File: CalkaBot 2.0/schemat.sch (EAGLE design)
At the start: 41 parts, among them IC1 TB6612FNG, IC2 LM339D, Q1 16MHz, X1 MINI-USB-32005-301

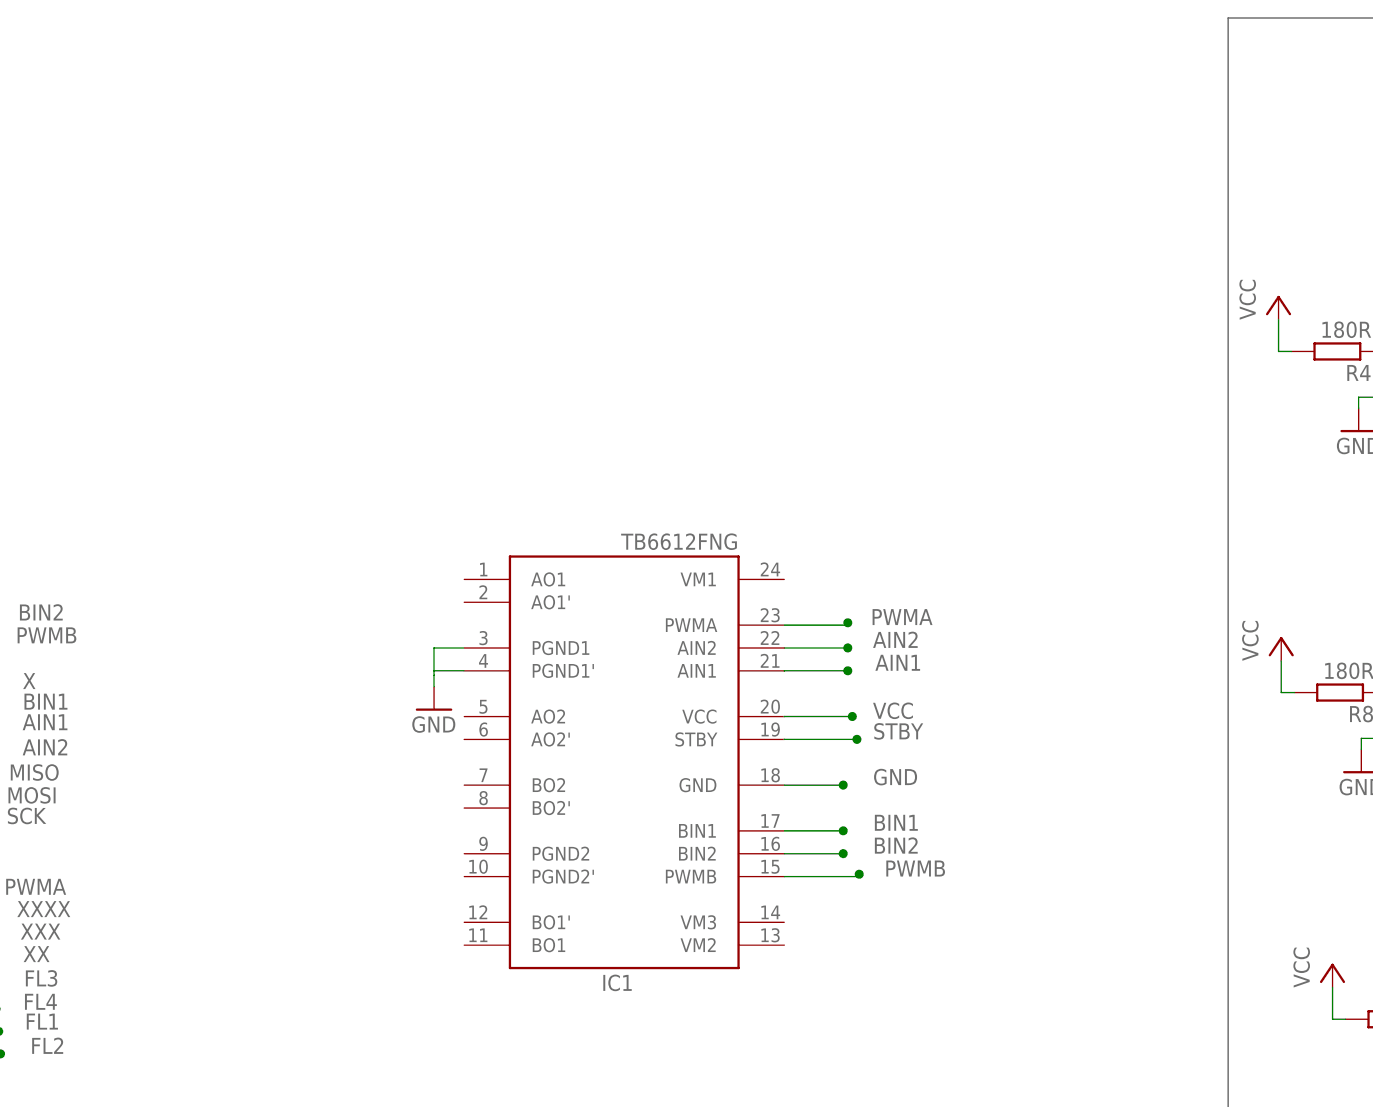
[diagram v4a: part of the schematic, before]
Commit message: Dodałem filtr do zasialania silników i do sterownika
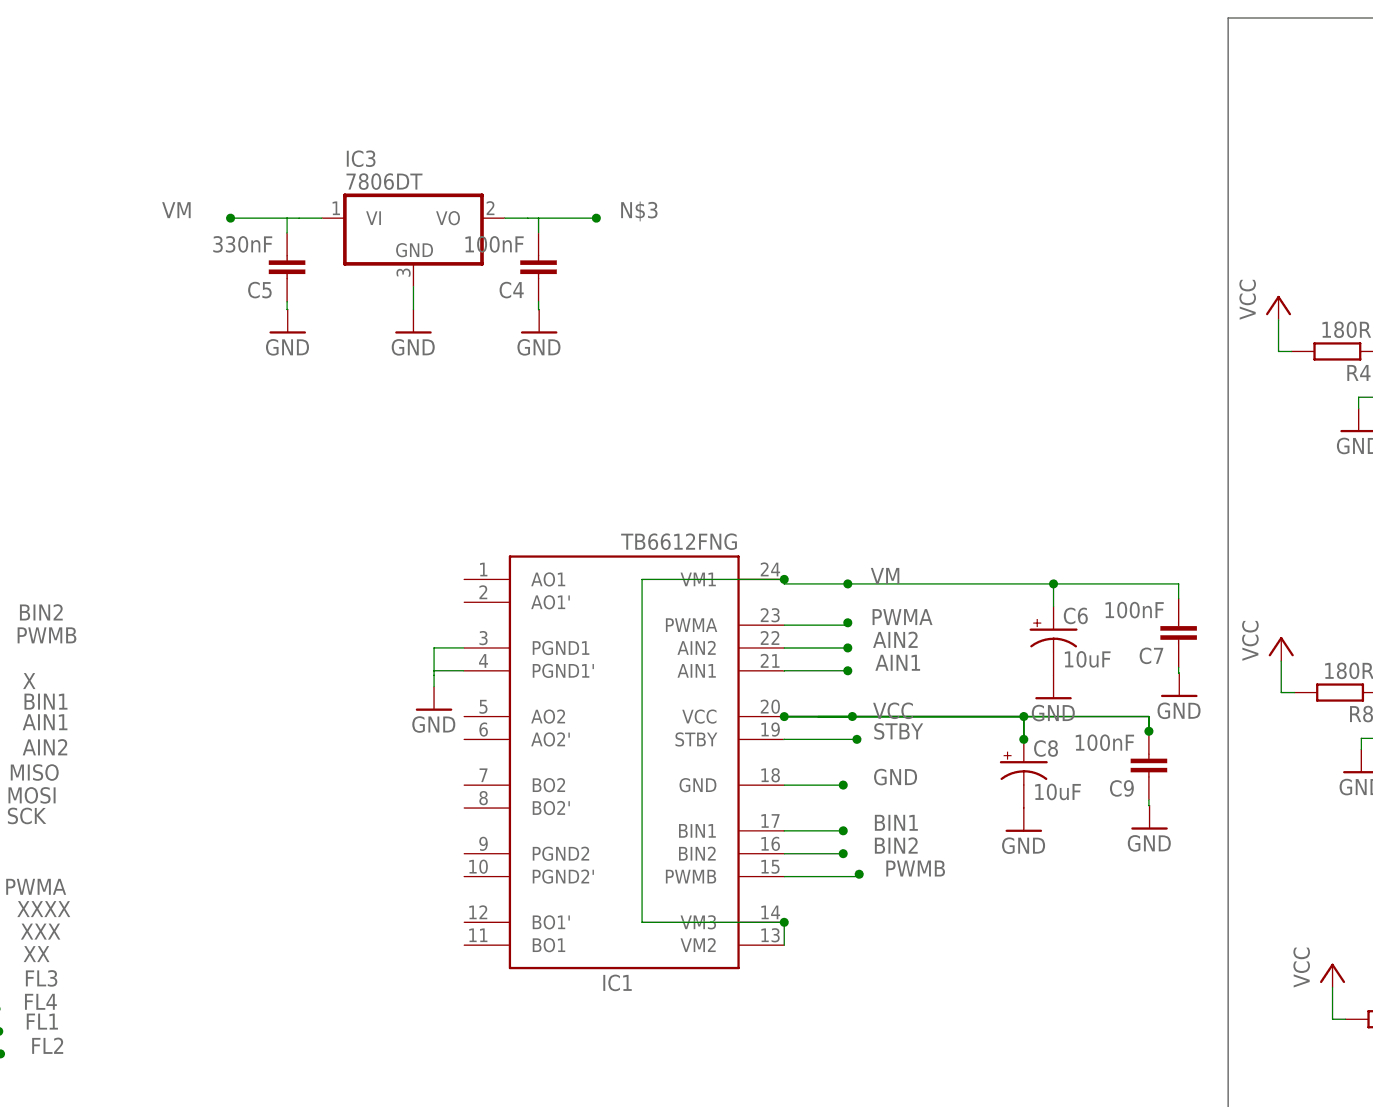
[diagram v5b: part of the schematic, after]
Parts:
- added C4, C7, C9: 100nF, rcl:C-EUC0805
- added C5: 330nF, rcl:C-EUC0805
- added C6, C8: 10uF, rcl:CPOL-USUD-4X5,8
- added IC3: 7806DT, linear3:7806DT
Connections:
- new net N$3: C4.2, IC3.VO
- new net VM: C5.2, C6.+, C7.2, IC1.VM1, IC1.VM2, IC1.VM3, IC3.VI
- net GND: now also C4.1, C5.1, C6.-, C7.1, C8.-, C9.1, IC3.GND
- net VCC: now also C8.+, C9.2
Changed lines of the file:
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@@
 <part name="R9" library="rcl" library_urn="urn:adsk.eagle:library:334" deviceset="R-EU_" device="R0805" package3d_urn="urn:adsk.eagle:package:23553/2" value="10k"/>
 <part name="RESETBUTTON3" library="switch-omron" library_urn="urn:adsk.eagle:library:377" deviceset="10-XX" device="" package3d_urn="urn:adsk.eagle:package:27496/1"/>
+<part name="IC3" library="linear3" deviceset="78*" device="DT" technology="06"/>
+<part name="GND7" library="supply1" library_urn="urn:adsk.eagle:library:371" deviceset="GND" device=""/>
+<part name="C4" library="rcl" library_urn="urn:adsk.eagle:library:334" deviceset="C-EU" device="C0805" package3d_urn="urn:adsk.eagle:package:23617/2" value="100nF"/>
+<part name="C5" library="rcl" library_urn="urn:adsk.eagle:library:334" deviceset="C-EU" device="C0805" package3d_urn="urn:adsk.eagle:package:23617/2" value="330nF"/>
+<part name="GND10" library="supply1" library_urn="urn:adsk.eagle:library:371" deviceset="GND" device=""/>
+<part name="GND13" library="supply1" library_urn="urn:adsk.eagle:library:371" deviceset="GND" device=""/>
+<part name="C6" library="rcl" library_urn="urn:adsk.eagle:library:334" deviceset="CPOL-US" device="UD-4X5,8" package3d_urn="urn:adsk.eagle:package:23474/1" value="10uF"/>
+<part name="C7" library="rcl" library_urn="urn:adsk.eagle:library:334" deviceset="C-EU" device="C0805" package3d_urn="urn:adsk.eagle:package:23617/2" value="100nF"/>
+<part name="GND14" library="supply1" library_urn="urn:adsk.eagle:library:371" deviceset="GND" device=""/>
+<part name="GND15" library="supply1" library_urn="urn:adsk.eagle:library:371" deviceset="GND" device=""/>
+<part name="C8" library="rcl" library_urn="urn:adsk.eagle:library:334" deviceset="CPOL-US" device="UD-4X5,8" package3d_urn="urn:adsk.eagle:package:23474/1" value="10uF"/>
+<part name="C9" library="rcl" library_urn="urn:adsk.eagle:library:334" deviceset="C-EU" device="C0805" package3d_urn="urn:adsk.eagle:package:23617/2" value="100nF"/>
+<part name="GND16" library="supply1" library_urn="urn:adsk.eagle:library:371" deviceset="GND" device=""/>
+<part name="GND17" library="supply1" library_urn="urn:adsk.eagle:library:371" deviceset="GND" device=""/>
 </parts>
 <sheets>
@@
 <instance part="R9" gate="G$1" x="21.082" y="-0.508"/>
 <instance part="RESETBUTTON3" gate="1" x="21.22" y="-10.26" rot="R90"/>
+<instance part="IC3" gate="A1" x="68.58" y="124.46"/>
+<instance part="GND7" gate="1" x="68.58" y="111.76"/>
+<instance part="C4" gate="G$1" x="82.48" y="117.74" rot="R180"/>
+<instance part="C5" gate="G$1" x="54.54" y="117.74" rot="R180"/>
+<instance part="GND10" gate="1" x="82.55" y="111.76"/>
+<instance part="GND13" gate="1" x="54.61" y="111.76"/>
+<instance part="C6" gate="G$1" x="139.7" y="78.74"/>
+<instance part="C7" gate="G$1" x="153.6" y="77.1" rot="R180"/>
+<instance part="GND14" gate="1" x="139.7" y="71.12"/>
+<instance part="GND15" gate="1" x="153.67" y="71.374"/>
+<instance part="C8" gate="G$1" x="136.398" y="64.008"/>
+<instance part="C9" gate="G$1" x="150.298" y="62.368" rot="R180"/>
+<instance part="GND16" gate="1" x="136.398" y="56.388"/>
+<instance part="GND17" gate="1" x="150.368" y="56.642"/>
 </instances>
 <busses>
@@
 <junction x="-93.08" y="-7.72"/>
 </segment>
+<segment>
+<pinref part="IC3" gate="A1" pin="GND"/>
+<wire x1="68.58" y1="116.84" x2="68.58" y2="114.3" width="0.1524" layer="91"/>
+<pinref part="GND7" gate="1" pin="GND"/>
+</segment>
+<segment>
+<pinref part="GND13" gate="1" pin="GND"/>
+<pinref part="C5" gate="G$1" pin="1"/>
+<wire x1="54.61" y1="114.3" x2="54.54" y2="114.3" width="0.1524" layer="91"/>
+<wire x1="54.54" y1="114.3" x2="54.54" y2="115.2" width="0.1524" layer="91"/>
+</segment>
+<segment>
+<pinref part="GND10" gate="1" pin="GND"/>
+<pinref part="C4" gate="G$1" pin="1"/>
+<wire x1="82.55" y1="114.3" x2="82.48" y2="114.3" width="0.1524" layer="91"/>
+<wire x1="82.48" y1="114.3" x2="82.48" y2="115.2" width="0.1524" layer="91"/>
+</segment>
+<segment>
+<pinref part="C6" gate="G$1" pin="-"/>
+<pinref part="GND14" gate="1" pin="GND"/>
+</segment>
+<segment>
+<pinref part="C7" gate="G$1" pin="1"/>
+<pinref part="GND15" gate="1" pin="GND"/>
+<wire x1="153.6" y1="74.56" x2="153.6" y2="73.914" width="0.1524" layer="91"/>
+<wire x1="153.6" y1="73.914" x2="153.67" y2="73.914" width="0.1524" layer="91"/>
+</segment>
+<segment>
+<pinref part="C8" gate="G$1" pin="-"/>
+<pinref part="GND16" gate="1" pin="GND"/>
+</segment>
+<segment>
+<pinref part="C9" gate="G$1" pin="1"/>
+<pinref part="GND17" gate="1" pin="GND"/>
+<wire x1="150.298" y1="59.828" x2="150.298" y2="59.182" width="0.1524" layer="91"/>
+<wire x1="150.298" y1="59.182" x2="150.368" y2="59.182" width="0.1524" layer="91"/>
+</segment>
 </net>
 <net name="D-" class="0">
@@
 <junction x="117.348" y="69.088"/>
 <label x="119.634" y="68.834" size="1.778" layer="95"/>
+<wire x1="109.78" y1="69.08" x2="139.7" y2="69.08" width="0.1524" layer="91"/>
+<wire x1="113.538" y1="69.088" x2="136.398" y2="69.088" width="0.1524" layer="91"/>
+<wire x1="136.398" y1="69.088" x2="150.298" y2="69.088" width="0.1524" layer="91"/>
+<wire x1="136.398" y1="69.088" x2="136.398" y2="66.548" width="0.1524" layer="91"/>
+<junction x="136.398" y="69.088"/>
+<pinref part="C8" gate="G$1" pin="+"/>
+<pinref part="C9" gate="G$1" pin="2"/>
+<wire x1="150.298" y1="67.448" x2="150.298" y2="69.088" width="0.1524" layer="91"/>
+<wire x1="109.78" y1="69.08" x2="136.398" y2="69.08" width="0.1524" layer="91"/>
+<wire x1="136.398" y1="69.08" x2="136.398" y2="66.548" width="0.1524" layer="91"/>
+<junction x="109.78" y="69.08"/>
+<junction x="136.398" y="66.548"/>
+<wire x1="109.78" y1="69.08" x2="150.298" y2="69.08" width="0.1524" layer="91"/>
+<wire x1="150.298" y1="69.08" x2="150.298" y2="67.448" width="0.1524" layer="91"/>
+<junction x="150.298" y="67.448"/>
 </segment>
 <segment>
@@
 </segment>
 </net>
+<net name="N$3" class="0">
+<segment>
+<pinref part="IC3" gate="A1" pin="VO"/>
+<pinref part="C4" gate="G$1" pin="2"/>
+<wire x1="78.74" y1="124.46" x2="81.28" y2="124.46" width="0.1524" layer="91"/>
+<wire x1="81.28" y1="124.46" x2="82.48" y2="124.46" width="0.1524" layer="91"/>
+<wire x1="82.48" y1="124.46" x2="82.48" y2="122.82" width="0.1524" layer="91"/>
+<wire x1="82.48" y1="124.46" x2="88.9" y2="124.46" width="0.1524" layer="91"/>
+<junction x="88.9" y="124.46"/>
+<label x="91.44" y="124.46" size="1.778" layer="95"/>
+</segment>
+</net>
+<net name="VM" class="0">
+<segment>
+<pinref part="C5" gate="G$1" pin="2"/>
+<pinref part="IC3" gate="A1" pin="VI"/>
+<wire x1="54.54" y1="122.82" x2="54.54" y2="124.46" width="0.1524" layer="91"/>
+<wire x1="54.54" y1="124.46" x2="55.88" y2="124.46" width="0.1524" layer="91"/>
+<wire x1="55.88" y1="124.46" x2="58.42" y2="124.46" width="0.1524" layer="91"/>
+<wire x1="54.54" y1="124.46" x2="48.26" y2="124.46" width="0.1524" layer="91"/>
+<junction x="48.26" y="124.46"/>
+<label x="40.64" y="124.46" size="1.778" layer="95"/>
+</segment>
+<segment>
+<pinref part="IC1" gate="G$1" pin="VM1"/>
+<wire x1="109.78" y1="84.32" x2="109.78" y2="83.82" width="0.1524" layer="91"/>
+<wire x1="109.78" y1="83.82" x2="116.84" y2="83.82" width="0.1524" layer="91"/>
+<junction x="116.84" y="83.82"/>
+<label x="119.38" y="83.82" size="1.778" layer="95"/>
+<wire x1="116.84" y1="83.82" x2="139.7" y2="83.82" width="0.1524" layer="91"/>
+<wire x1="139.7" y1="83.82" x2="153.6" y2="83.82" width="0.1524" layer="91"/>
+<wire x1="139.7" y1="83.82" x2="139.7" y2="81.28" width="0.1524" layer="91"/>
+<junction x="139.7" y="83.82"/>
+<pinref part="C6" gate="G$1" pin="+"/>
+<pinref part="C7" gate="G$1" pin="2"/>
+<wire x1="153.6" y1="82.18" x2="153.6" y2="83.82" width="0.1524" layer="91"/>
+<wire x1="109.78" y1="84.32" x2="93.98" y2="84.32" width="0.1524" layer="91"/>
+<junction x="109.78" y="84.32"/>
+<pinref part="IC1" gate="G$1" pin="VM2"/>
+<pinref part="IC1" gate="G$1" pin="VM3"/>
+<wire x1="109.78" y1="46.22" x2="109.78" y2="43.68" width="0.1524" layer="91"/>
+<wire x1="93.98" y1="84.32" x2="93.98" y2="46.22" width="0.1524" layer="91"/>
+<wire x1="93.98" y1="46.22" x2="109.78" y2="46.22" width="0.1524" layer="91"/>
+<junction x="109.78" y="46.22"/>
+</segment>
+</net>
